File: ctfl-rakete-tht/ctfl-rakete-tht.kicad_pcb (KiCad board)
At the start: 2 copper layers, 99.8 x 99.4 mm, 31 parts, among them J1 Conn_02x03_Odd_Even, SW1 SW_SPDT, U1 ATtiny212-SS

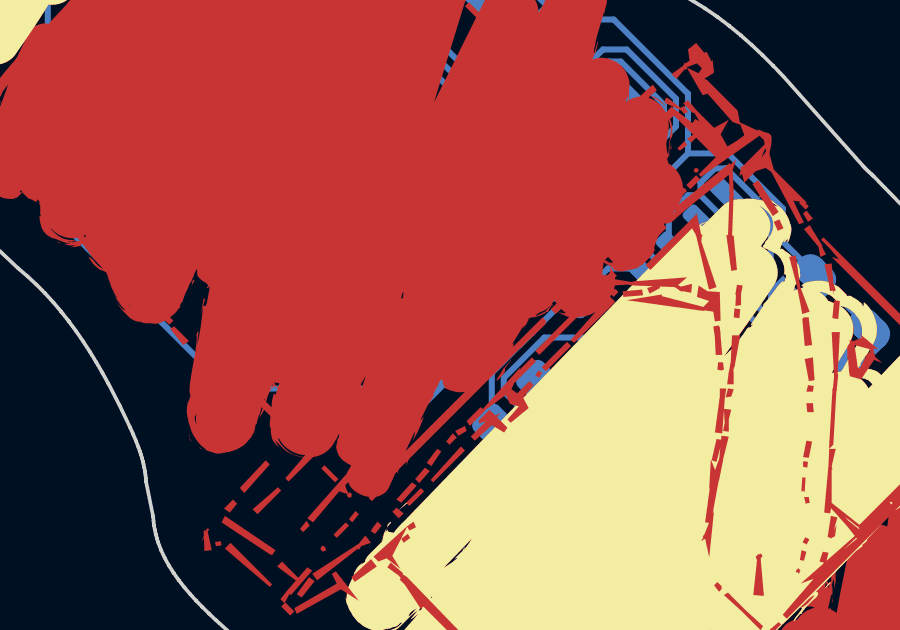
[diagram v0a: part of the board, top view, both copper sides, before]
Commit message: added a second decoupling capacitor with 1 uF to the Controller supply
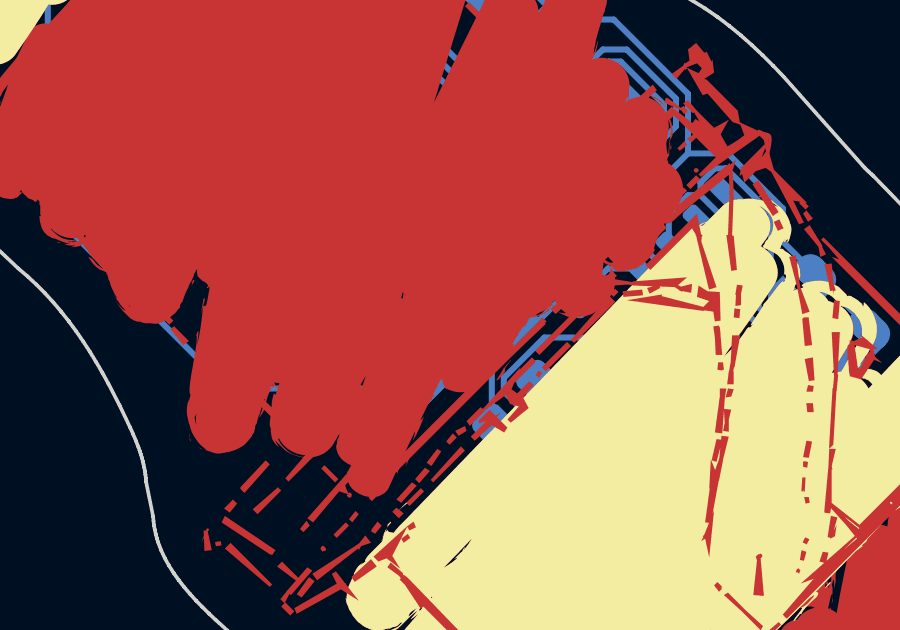
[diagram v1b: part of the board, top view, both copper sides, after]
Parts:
- added C3: 1u, Capacitor_SMD:C_0805_2012Metric_Pad1.18x1.45mm_HandSolder, B.Cu at (148.6, 95.2)
- moved JP1 0.99 mm to (145.8, 92.8)
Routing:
- net GND: track 196.7 -> 194.7 mm
- net +3V0: track 58.5 -> 60.1 mm

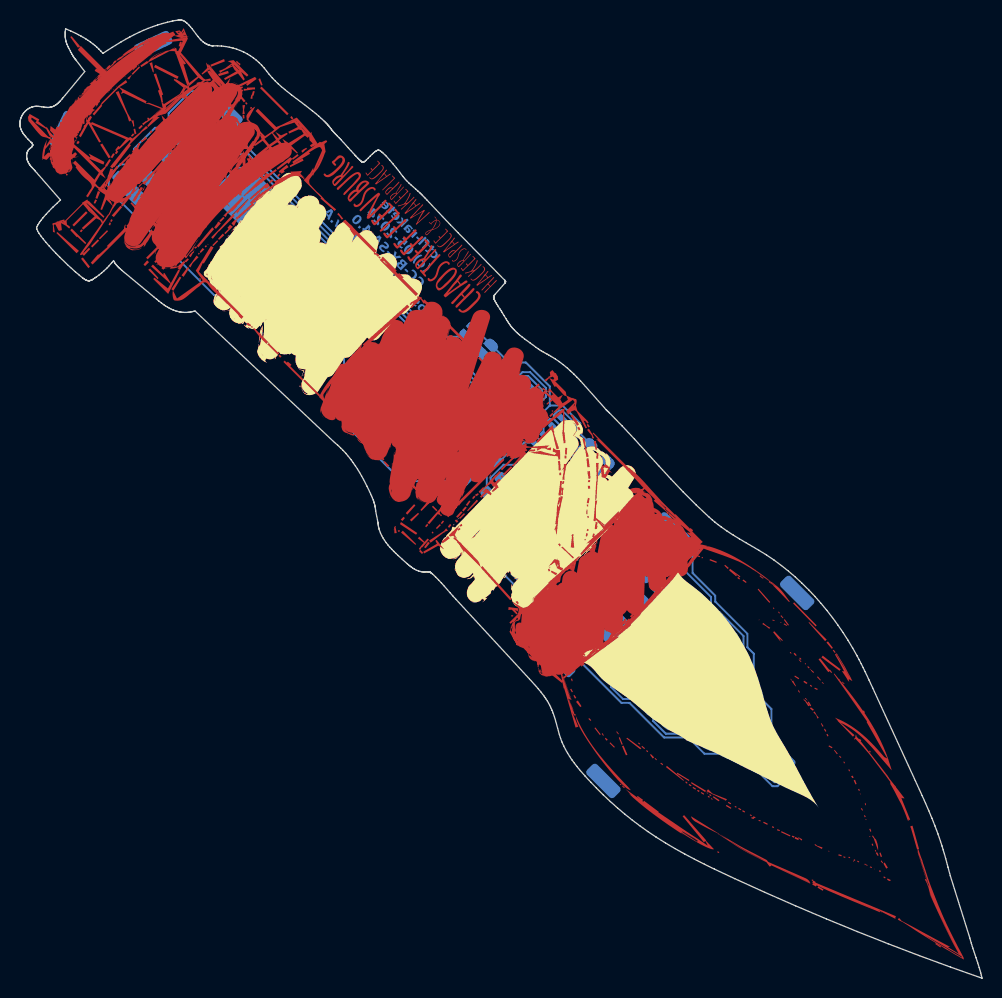
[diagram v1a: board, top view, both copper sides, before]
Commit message: updated to use design with new name 'Chaos Computer Club Flensburg E.V.'
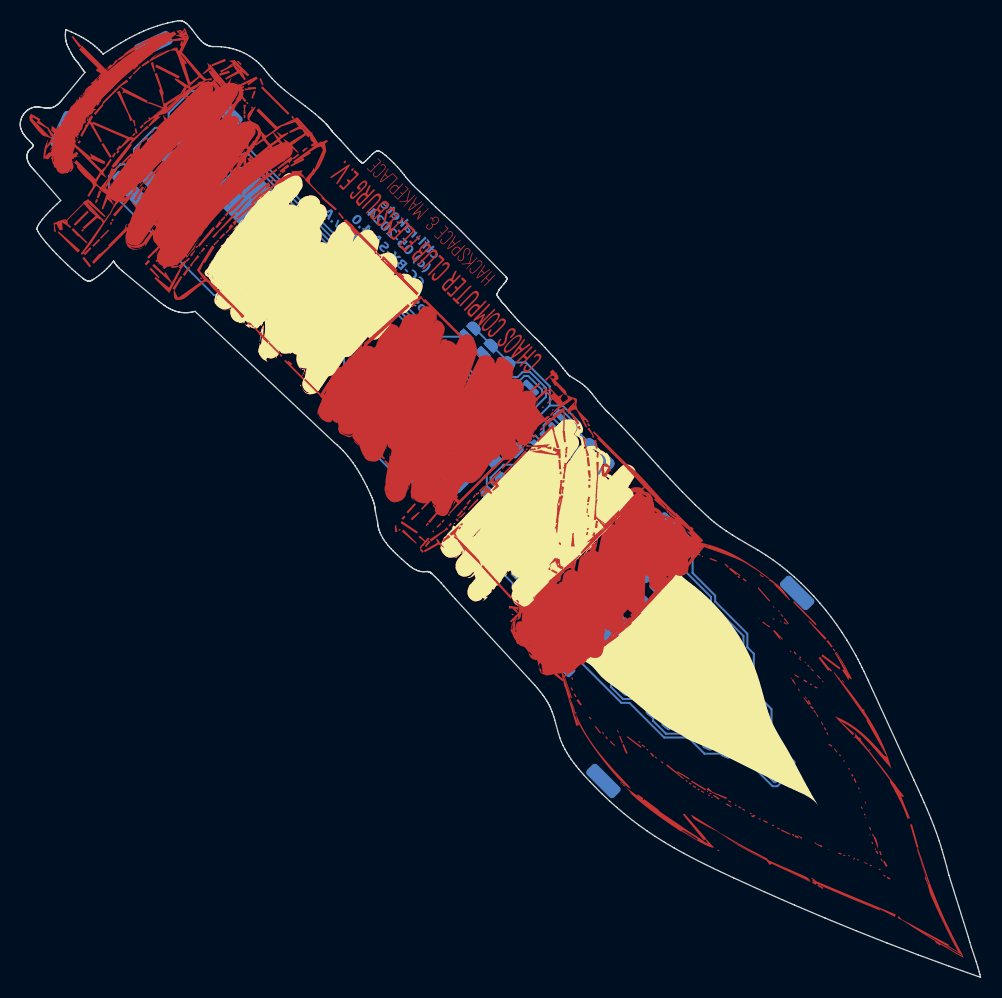
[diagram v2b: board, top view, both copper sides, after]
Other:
- board size 99.8 x 99.4 mm -> 99.6 x 99.2 mm
